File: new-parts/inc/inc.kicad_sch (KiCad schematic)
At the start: 20 parts, among them J1 BHR-10-VUA, J2 BHR-10-VUA, J3 Conn_01x02, J4 Conn_01x01, K1 J104D2C12VDC.15S, K2 J104D2C12VDC.15S, K3 J104D2C12VDC.15S, K4 J104D2C12VDC.15S, K5 J104D2C12VDC.15S, K6 J104D2C12VDC.15S, K7 J104D2C12VDC.15S, K8 J104D2C12VDC.15S

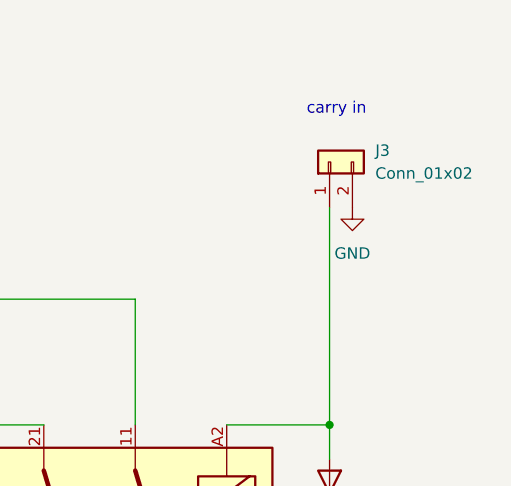
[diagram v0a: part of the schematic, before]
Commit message: Change all two-pin headers for control + ground to control only.
This is to prevent accidental short circuits when they are plugged in the
wrong way.
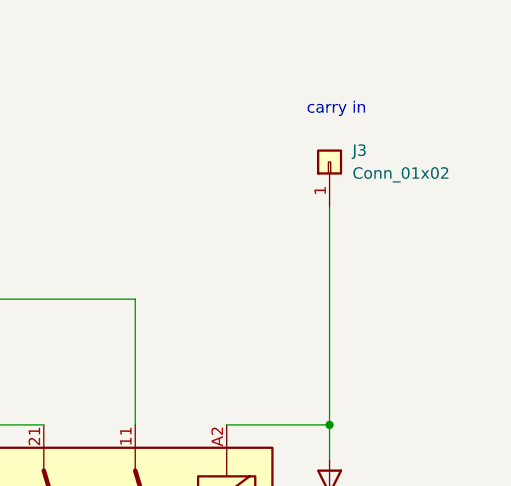
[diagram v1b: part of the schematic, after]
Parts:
- J3: footprint Connector_PinHeader_2.54mm:PinHeader_1x02_P2.54mm_Vertical -> Connector_PinHeader_2.54mm:PinHeader_1x01_P2.54mm_Vertical; symbol Connector_Generic:Conn_01x02 -> Connector_Generic:Conn_01x01
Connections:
- net GND: no longer J3.2 (Pin_2)
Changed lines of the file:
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@@
     )
   )
-  (symbol (lib_id "Connector_Generic:Conn_01x02") (at 388.62 74.93 90) (unit 1)
-    (in_bom yes) (on_board yes) (dnp no) (fields_autoplaced)
-    (property "Reference" "J3" (at 393.7 73.66 90)
+  (symbol (lib_id "Connector_Generic:Conn_01x01") (at 388.62 74.93 90) (unit 1)
+    (in_bom yes) (on_board yes) (dnp no) (fields_autoplaced)
+    (property "Reference" "J3" (at 391.16 73.66 90)
       (effects (font (size 1.27 1.27)) (justify right))
     )
-    (property "Value" "Conn_01x02" (at 393.7 76.2 90)
+    (property "Value" "Conn_01x02" (at 391.16 76.2 90)
       (effects (font (size 1.27 1.27)) (justify right))
     )
-    (property "Footprint" "Connector_PinHeader_2.54mm:PinHeader_1x02_P2.54mm_Vertical" (at 388.62 74.93 0)
+    (property "Footprint" "Connector_PinHeader_2.54mm:PinHeader_1x01_P2.54mm_Vertical" (at 388.62 74.93 0)
       (effects (font (size 1.27 1.27)) hide)
     )
@@
     )
     (pin "1")
-    (pin "2")
     (instances
       (project "inc"
@@
         )
       )
-    )
-  )
-  (symbol (lib_id "power:GND") (at 391.16 80.01 0) (unit 1)
-    (in_bom yes) (on_board yes) (dnp no) (fields_autoplaced)
-    (property "Reference" "#PWR07" (at 391.16 86.36 0)
-      (effects (font (size 1.27 1.27)) hide)
-    )
-    (property "Value" "GND" (at 391.16 85.09 0)
-      (effects (font (size 1.27 1.27)))
-    )
-    (property "Footprint" "" (at 391.16 80.01 0)
-      (effects (font (size 1.27 1.27)) hide)
-    )
-    (property "Datasheet" "" (at 391.16 80.01 0)
-      (effects (font (size 1.27 1.27)) hide)
-    )
-    (pin "1")
-    (instances
-      (project "inc"
-        (path "/8e7358e7-c3ef-4f3e-9154-e7eba01c544e"
-          (reference "#PWR07") (unit 1)
-        )
-      )

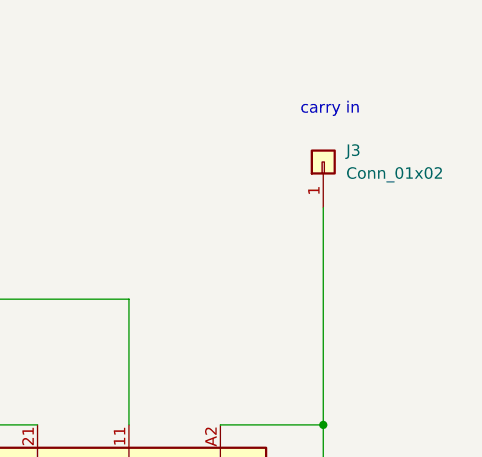
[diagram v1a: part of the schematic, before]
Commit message: Fix connector values: change names from 2 rows to 1 row.
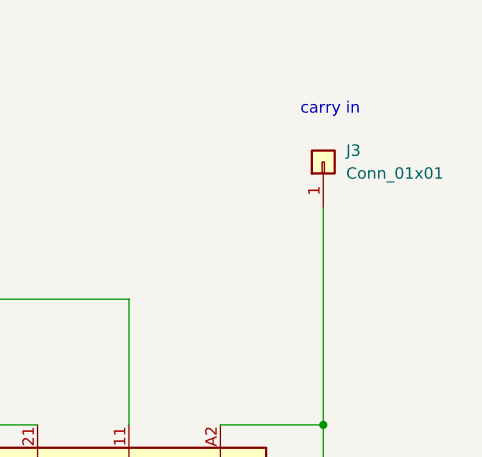
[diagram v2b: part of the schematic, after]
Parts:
- J3: value Conn_01x02 -> Conn_01x01
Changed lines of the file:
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@@
       (effects (font (size 1.27 1.27)) (justify right))
     )
-    (property "Value" "Conn_01x02" (at 391.16 76.2 90)
+    (property "Value" "Conn_01x01" (at 391.16 76.2 90)
       (effects (font (size 1.27 1.27)) (justify right))
     )
